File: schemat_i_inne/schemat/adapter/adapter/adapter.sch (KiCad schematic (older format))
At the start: 2 parts, among them J1 Conn_01x06_Female, J2 RJ45

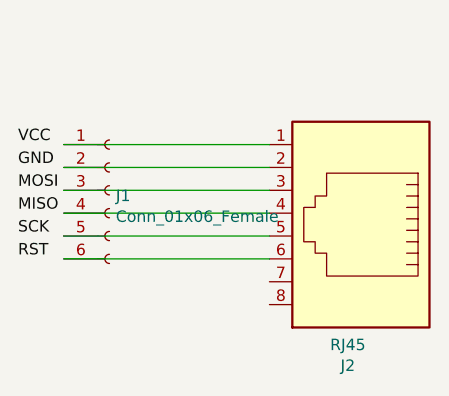
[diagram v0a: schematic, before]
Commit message: Upraszczanie polaczen i poprawianie plytki
Gotowe polaczenia do ekranu
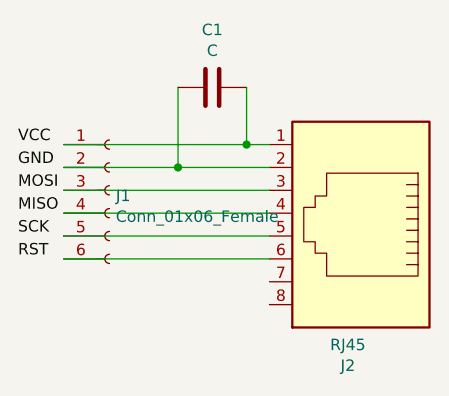
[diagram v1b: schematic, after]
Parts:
- added C1: C, Connector_PinHeader_2.54mm:PinHeader_1x02_P2.54mm_Vertical, symbol Device:C
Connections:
- net at J1.1 (Pin_1), J2.1: now also C1.1
- net at J1.2 (Pin_2), J2.2: now also C1.2
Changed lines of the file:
@@
 $EndComp
 Wire Wire Line
-	6150 3100 5250 3100
+	6150 3100 6050 3100
 Wire Wire Line
-	6150 3200 5250 3200
+	6150 3200 5750 3200
 Wire Wire Line
 	5250 3300 6150 3300
@@
 Text Label 5050 3600 0    50   ~ 0
 RST
+$Comp
+L Device:C C1
+U 1 1 627FB761
+P 5900 2850
+F 0 "C1" V 5648 2850 50  0000 C CNN
+F 1 "C" V 5739 2850 50  0000 C CNN
+F 2 "Connector_PinHeader_2.54mm:PinHeader_1x02_P2.54mm_Vertical" H 5938 2700 50  0001 C CNN
+F 3 "~" H 5900 2850 50  0001 C CNN
+	1    5900 2850
+	0    1    1    0
+$EndComp
+Wire Wire Line
+	5750 2850 5750 3200
+Connection ~ 5750 3200
+Wire Wire Line
+	5750 3200 5250 3200
+Wire Wire Line
+	6050 2850 6050 3100
+Connection ~ 6050 3100
+Wire Wire Line
+	6050 3100 5250 3100
 $EndSCHEMATC

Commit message: Koncowe sciezki i adapter
Ukonczono poprawianie sciezek i poprawnie zrobiono adapter
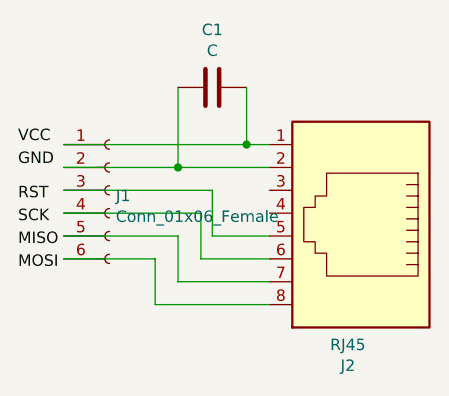
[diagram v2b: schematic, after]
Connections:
- net at J2.3: no longer J1.3 (Pin_3)
- net at J2.4: no longer J1.4 (Pin_4)
- net at J2.5: now also J1.3 (Pin_3); no longer J1.5 (Pin_5)
- net at J2.6: now also J1.4 (Pin_4); no longer J1.6 (Pin_6)
- net at J2.7: now also J1.5 (Pin_5)
- net at J2.8: now also J1.6 (Pin_6)
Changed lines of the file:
@@
 	-1   0    0    1
-$EndComp
-$Comp
-L Connector:Conn_01x06_Female J1
-U 1 1 62A94AE0
-P 5450 3300
-F 0 "J1" H 5478 3276 50  0000 L CNN
-F 1 "Conn_01x06_Female" H 5478 3185 50  0000 L CNN
-F 2 "Connector_PinHeader_2.54mm:PinHeader_1x06_P2.54mm_Vertical" H 5450 3300 50  0001 C CNN
-F 3 "~" H 5450 3300 50  0001 C CNN
-	1    5450 3300
-	1    0    0    -1
 $EndComp
 Wire Wire Line
@@
 Wire Wire Line
 	6150 3200 5750 3200
-Wire Wire Line
-	5250 3300 6150 3300
-Wire Wire Line
-	6150 3400 5250 3400
-Wire Wire Line
-	6150 3500 5250 3500
-Wire Wire Line
-	6150 3600 5250 3600
 Text Label 5050 3100 0    50   ~ 0
 VCC
 Text Label 5050 3200 0    50   ~ 0
 GND
-Text Label 5050 3300 0    50   ~ 0
+Text Label 5050 3650 0    50   ~ 0
 MOSI
-Text Label 5050 3400 0    50   ~ 0
+Text Label 5050 3550 0    50   ~ 0
 MISO
-Text Label 5050 3500 0    50   ~ 0
+Text Label 5050 3450 0    50   ~ 0
 SCK
-Text Label 5050 3600 0    50   ~ 0
+Text Label 5050 3350 0    50   ~ 0
 RST
 $Comp
@@
 Wire Wire Line
 	6050 3100 5250 3100
+$Comp
+L Connector:Conn_01x06_Female J1
+U 1 1 62A94AE0
+P 5450 3300
+F 0 "J1" H 5478 3276 50  0000 L CNN
+F 1 "Conn_01x06_Female" H 5478 3185 50  0000 L CNN
+F 2 "Connector_PinHeader_2.54mm:PinHeader_1x06_P2.54mm_Vertical" H 5450 3300 50  0001 C CNN
+F 3 "~" H 5450 3300 50  0001 C CNN
+	1    5450 3300
+	1    0    0    -1
+$EndComp
+Wire Wire Line
+	5250 3300 5900 3300
+Wire Wire Line
+	5900 3300 5900 3500
+Wire Wire Line
+	5900 3500 6150 3500
+Wire Wire Line
+	5850 3400 5850 3600
+Wire Wire Line
+	5850 3600 6150 3600
+Wire Wire Line
+	5250 3500 5750 3500
+Wire Wire Line
+	5750 3500 5750 3700
+Wire Wire Line
+	5750 3700 6150 3700
+Wire Wire Line
+	5250 3600 5650 3600
+Wire Wire Line
+	5650 3600 5650 3800
+Wire Wire Line
+	5650 3800 6150 3800
+Wire Wire Line
+	5250 3400 5850 3400
 $EndSCHEMATC
